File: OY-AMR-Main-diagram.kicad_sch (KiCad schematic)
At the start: 2 parts

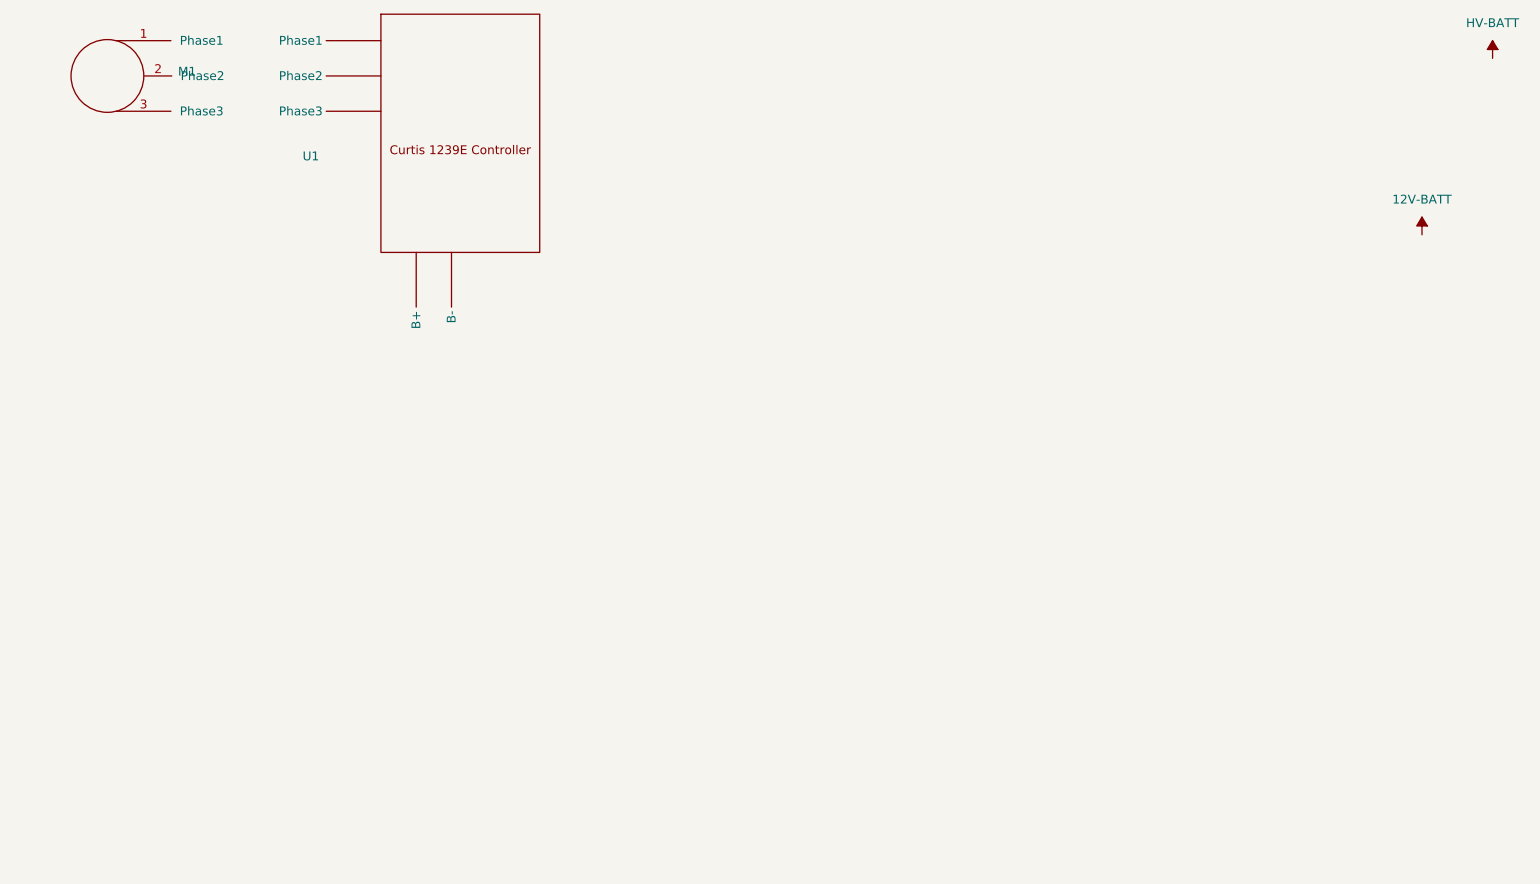
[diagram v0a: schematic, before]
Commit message: Added key switch component
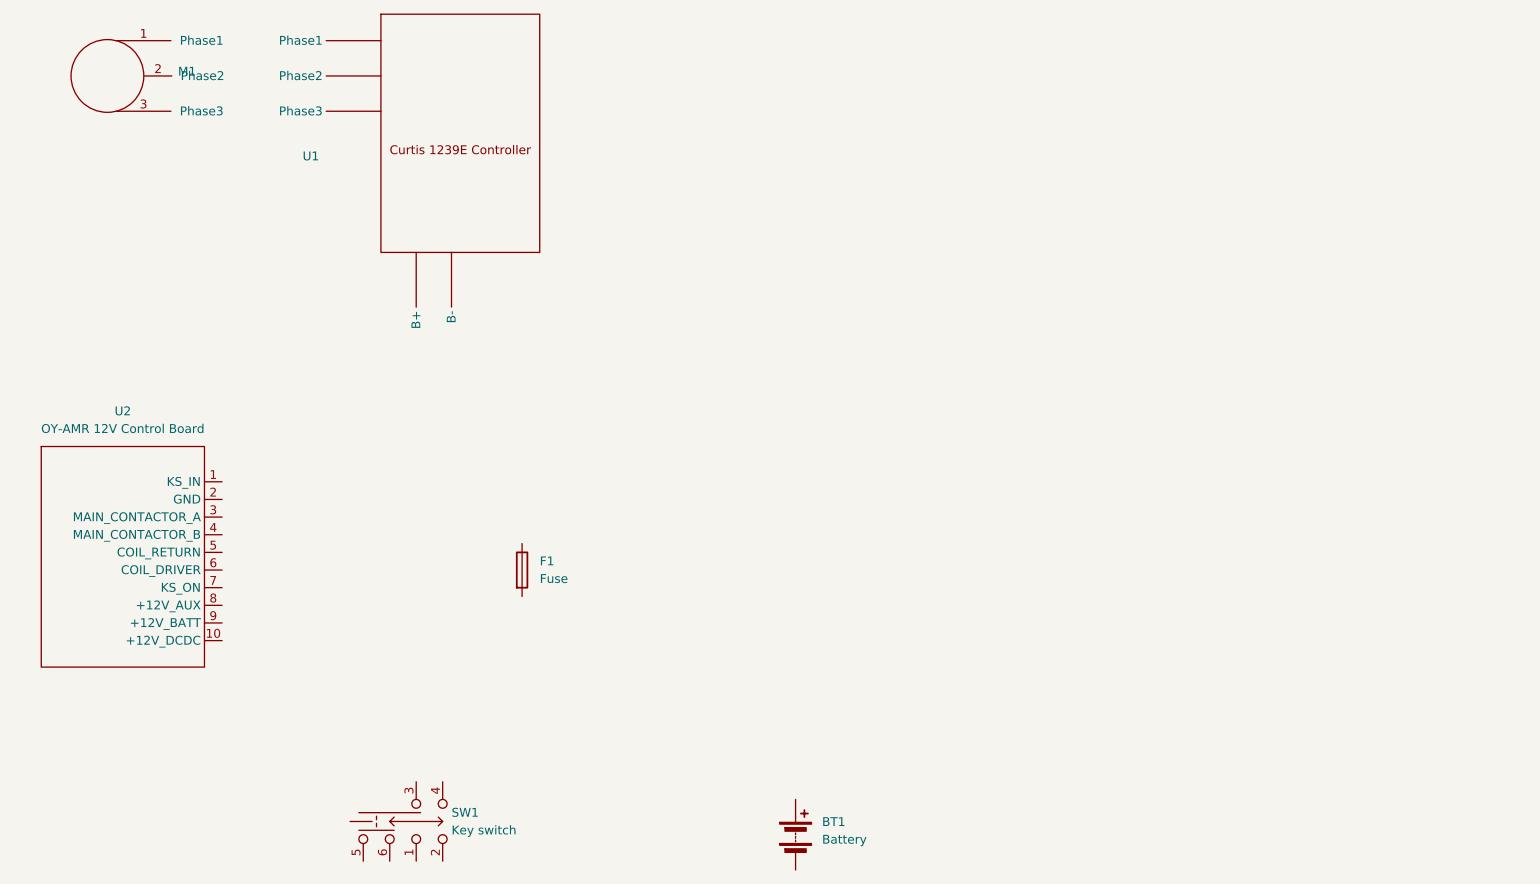
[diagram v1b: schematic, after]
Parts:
- added BT1: Battery, symbol Device:Battery
- added F1: Fuse, symbol Device:Fuse
- added SW1: Key switch, symbol OYAMR_Library:89165-01
- added U2: OY-AMR 12V Control Board, https://github.com/elfremdrift/OY-AMR-12V, symbol OYAMR_Library:Control_Board
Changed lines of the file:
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@@
 	(paper "A4")
+	(symbol
+		(lib_id "OYAMR_Library:Control_Board")
+		(at 52.07 92.71 0)
+		(unit 1)
+		(exclude_from_sim no)
+		(in_bom yes)
+		(on_board yes)
+		(dnp no)
+		(fields_autoplaced yes)
+		(property "Reference" "U2"
+			(at 46.6725 83.82 0)
+			(effects
+				(font
+					(size 1.27 1.27)
+				)
+			)
+		)
+		(property "Value" "OY-AMR 12V Control Board"
+			(at 46.6725 86.36 0)
+			(effects
+				(font
+					(size 1.27 1.27)
+				)
+			)
+		)
+		(property "Footprint" "https://github.com/elfremdrift/OY-AMR-12V"
+			(at 52.07 92.71 0)
+			(effects
+				(font
+					(size 1.27 1.27)
+				)
+				(hide yes)
+			)
+		)
+		(property "Datasheet" ""
+			(at 52.07 92.71 0)
+			(effects
+				(font
+					(size 1.27 1.27)
+				)
+				(hide yes)
+			)
+		)
+		(property "Description" ""
+			(at 52.07 92.71 0)
+			(effects
+				(font
+					(size 1.27 1.27)
+				)
+				(hide yes)
+			)
+		)
+		(pin "8"
+		)
+		(pin "3"
+		)
+		(pin "5"
+		)
+		(pin "7"
+		)
+		(pin "6"
+		)
+		(pin "4"
+		)
+		(pin "1"
+		)
+		(pin "2"
+		)
+		(pin "10"
+		)
+		(pin "9"
+		)
+		(instances
+			(project ""
+				(path "/ef01d6f9-a0de-44a4-9cac-f1674149af30"
+					(reference "U2")
+					(unit 1)
+				)
+			)
+		)
+	)
 	(symbol
 		(lib_id "OYAMR_Library:3_Phase_Motor")
@@
 	)
 	(symbol
-		(lib_id "power:-BATT")
-		(at 233.68 58.42 0)
-		(unit 1)
-		(exclude_from_sim no)
-		(in_bom yes)
-		(on_board yes)
-		(dnp no)
-		(fields_autoplaced yes)
-		(property "Reference" "#PWR02"
-			(at 233.68 62.23 0)
-			(effects
-				(font
-					(size 1.27 1.27)
-				)
-				(hide yes)
-			)
-		)
-		(property "Value" "12V-BATT"
-			(at 233.68 53.34 0)
-			(effects
-				(font
-					(size 1.27 1.27)
-				)
+		(lib_id "Device:Battery")
+		(at 143.51 144.78 0)
+		(unit 1)
+		(exclude_from_sim no)
+		(in_bom yes)
+		(on_board yes)
+		(dnp no)
+		(fields_autoplaced yes)
+		(property "Reference" "BT1"
+			(at 147.32 142.9384 0)
+			(effects
+				(font
+					(size 1.27 1.27)
+				)
+				(justify left)
+			)
+		)
+		(property "Value" "Battery"
+			(at 147.32 145.4784 0)
+			(effects
+				(font
+					(size 1.27 1.27)
+				)
+				(justify left)
 			)
 		)
 		(property "Footprint" ""
-			(at 233.68 58.42 0)
-			(effects
-				(font
-					(size 1.27 1.27)
-				)
-				(hide yes)
-			)
-		)
-		(property "Datasheet" ""
-			(at 233.68 58.42 0)
-			(effects
-				(font
-					(size 1.27 1.27)
-				)
-				(hide yes)
-			)
-		)
-		(property "Description" "Power symbol creates a global label with name \"-BATT\""
-			(at 233.68 58.42 0)
+			(at 143.51 143.256 90)
+			(effects
+				(font
+					(size 1.27 1.27)
+				)
+				(hide yes)
+			)
+		)
+		(property "Datasheet" "~"
+			(at 143.51 143.256 90)
+			(effects
+				(font
+					(size 1.27 1.27)
+				)
+				(hide yes)
+			)
+		)
+		(property "Description" "Multiple-cell battery"
+			(at 143.51 144.78 0)
 			(effects
 				(font
@@
 		(pin "1"
 		)
-		(instances
-			(project ""
-				(path "/ef01d6f9-a0de-44a4-9cac-f1674149af30"
-					(reference "#PWR02")
+		(pin "2"
+		)
+		(instances
+			(project ""
+				(path "/ef01d6f9-a0de-44a4-9cac-f1674149af30"
+					(reference "BT1")
+					(unit 1)
+				)
+			)
+		)
+	)
+	(symbol
+		(lib_id "Device:Fuse")
+		(at 104.14 106.68 0)
+		(unit 1)
+		(exclude_from_sim no)
+		(in_bom yes)
+		(on_board yes)
+		(dnp no)
+		(fields_autoplaced yes)
+		(property "Reference" "F1"
+			(at 106.68 105.4099 0)
+			(effects
+				(font
+					(size 1.27 1.27)
+				)
+				(justify left)
+			)
+		)
+		(property "Value" "Fuse"
+			(at 106.68 107.9499 0)
+			(effects
+				(font
+					(size 1.27 1.27)
+				)
+				(justify left)
+			)
+		)
+		(property "Footprint" ""
+			(at 102.362 106.68 90)
+			(effects
+				(font
+					(size 1.27 1.27)
+				)
+				(hide yes)
+			)
+		)
+		(property "Datasheet" "~"
+			(at 104.14 106.68 0)
+			(effects
+				(font
+					(size 1.27 1.27)
+				)
+				(hide yes)
+			)
+		)
+		(property "Description" "Fuse"
+			(at 104.14 106.68 0)
+			(effects
+				(font
+					(size 1.27 1.27)
+				)
+				(hide yes)
+			)
+		)
+		(pin "1"
+		)
+		(pin "2"
+		)
+		(instances
+			(project ""
+				(path "/ef01d6f9-a0de-44a4-9cac-f1674149af30"
+					(reference "F1")
+					(unit 1)
+				)
+			)
+		)
+	)
+	(symbol
+		(lib_id "OYAMR_Library:89165-01")
+		(at 87.63 143.51 0)
+		(unit 1)
+		(exclude_from_sim no)
+		(in_bom yes)
+		(on_board yes)
+		(dnp no)
+		(fields_autoplaced yes)
+		(property "Reference" "SW1"
+			(at 93.98 141.6049 0)
+			(effects
+				(font
+					(size 1.27 1.27)
+				)
+				(justify left)
+			)
+		)
+		(property "Value" "Key switch"
+			(at 93.98 144.1449 0)
+			(effects
+				(font
+					(size 1.27 1.27)
+				)
+				(justify left)
+			)
+		)
+		(property "Footprint" ""
+			(at 84.455 136.525 0)
+			(effects
+				(font
+					(size 1.27 1.27)
+				)
+				(hide yes)
+			)
+		)
+		(property "Datasheet" "~"
+			(at 84.455 136.525 0)
+			(effects
+				(font
+					(size 1.27 1.27)
+				)
+				(hide yes)
+			)
+		)
+		(property "Description" "Honywell key switch 6p off-on-start"
+			(at 87.63 143.51 0)
+			(effects
+				(font
+					(size 1.27 1.27)
+				)
+				(hide yes)
+			)
+		)
+		(pin "5"
+		)
+		(pin "2"
+		)
+		(pin "3"
+		)
+		(pin "4"
+		)
+		(pin "6"
+		)
+		(pin "1"
+		)
+		(instances
+			(project ""
+				(path "/ef01d6f9-a0de-44a4-9cac-f1674149af30"
+					(reference "SW1")
 					(unit 1)
 				)
@@
 					(unit 1)
 				)
-			)
-		)
-	)
-	(symbol
-		(lib_id "power:-BATT")
-		(at 243.84 33.02 0)
-		(unit 1)
-		(exclude_from_sim no)
-		(in_bom yes)
-		(on_board yes)
-		(dnp no)
-		(fields_autoplaced yes)
-		(property "Reference" "#PWR01"
-			(at 243.84 36.83 0)
-			(effects
-				(font
-					(size 1.27 1.27)
-				)
-				(hide yes)
-			)
-		)
-		(property "Value" "HV-BATT"
-			(at 243.84 27.94 0)
-			(effects
-				(font
-					(size 1.27 1.27)
-				)
-			)
-		)
-		(property "Footprint" ""
-			(at 243.84 33.02 0)
-			(effects
-				(font
-					(size 1.27 1.27)
-				)
-				(hide yes)
-			)
-		)
-		(property "Datasheet" ""
-			(at 243.84 33.02 0)
-			(effects
-				(font
-					(size 1.27 1.27)
-				)
-				(hide yes)
-			)
-		)
-		(property "Description" "Power symbol creates a global label with name \"-BATT\""
-			(at 243.84 33.02 0)
-			(effects
-				(font
-					(size 1.27 1.27)
-				)
-				(hide yes)
-			)
-		)
-		(pin "1"
-		)
-		(instances
-			(project ""
-				(path "/ef01d6f9-a0de-44a4-9cac-f1674149af30"
-					(reference "#PWR01")
-					(unit 1)
-				)

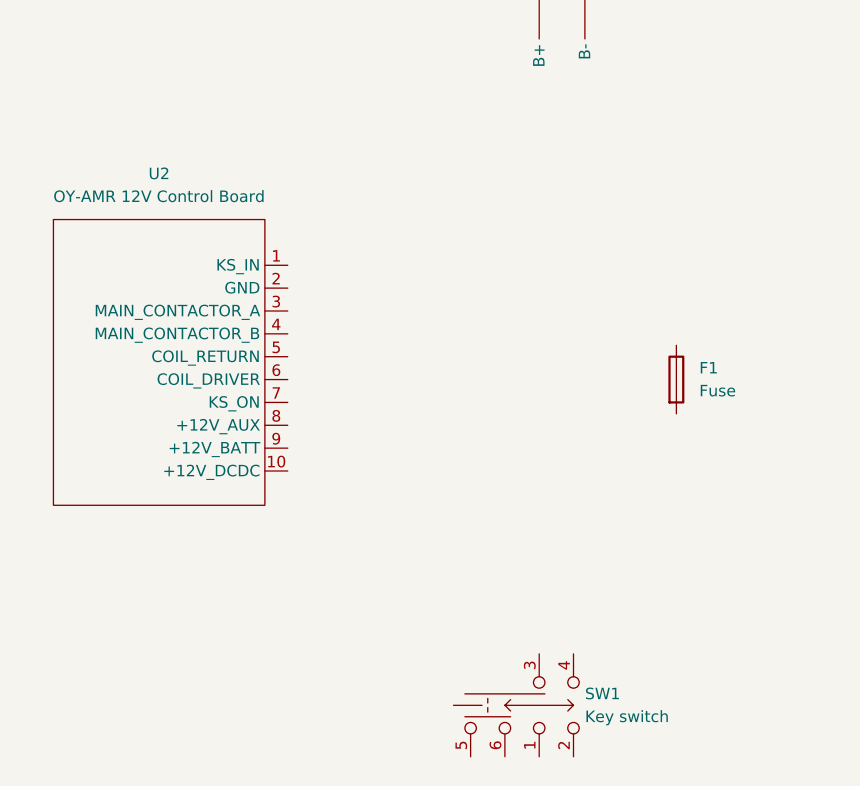
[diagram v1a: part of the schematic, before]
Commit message: removed unused comp.
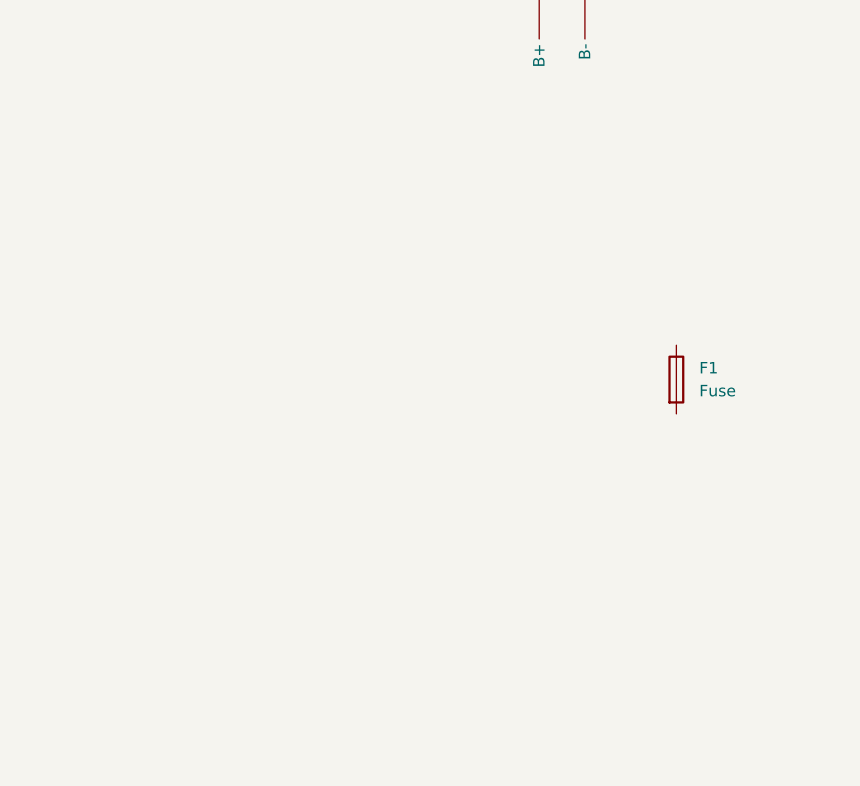
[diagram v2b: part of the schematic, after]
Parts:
- removed SW1: Key switch, symbol OYAMR_Library:89165-01
- removed U2: OY-AMR 12V Control Board, https://github.com/elfremdrift/OY-AMR-12V, symbol OYAMR_Library:Control_Board
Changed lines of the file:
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@@
 	(paper "A4")
-	(symbol
-		(lib_id "OYAMR_Library:Control_Board")
-		(at 52.07 92.71 0)
-		(unit 1)
-		(exclude_from_sim no)
-		(in_bom yes)
-		(on_board yes)
-		(dnp no)
-		(fields_autoplaced yes)
-		(property "Reference" "U2"
-			(at 46.6725 83.82 0)
-			(effects
-				(font
-					(size 1.27 1.27)
-				)
-			)
-		)
-		(property "Value" "OY-AMR 12V Control Board"
-			(at 46.6725 86.36 0)
-			(effects
-				(font
-					(size 1.27 1.27)
-				)
-			)
-		)
-		(property "Footprint" "https://github.com/elfremdrift/OY-AMR-12V"
-			(at 52.07 92.71 0)
-			(effects
-				(font
-					(size 1.27 1.27)
-				)
-				(hide yes)
-			)
-		)
-		(property "Datasheet" ""
-			(at 52.07 92.71 0)
-			(effects
-				(font
-					(size 1.27 1.27)
-				)
-				(hide yes)
-			)
-		)
-		(property "Description" ""
-			(at 52.07 92.71 0)
-			(effects
-				(font
-					(size 1.27 1.27)
-				)
-				(hide yes)
-			)
-		)
-		(pin "8"
-		)
-		(pin "3"
-		)
-		(pin "5"
-		)
-		(pin "7"
-		)
-		(pin "6"
-		)
-		(pin "4"
-		)
-		(pin "1"
-		)
-		(pin "2"
-		)
-		(pin "10"
-		)
-		(pin "9"
-		)
-		(instances
-			(project ""
-				(path "/ef01d6f9-a0de-44a4-9cac-f1674149af30"
-					(reference "U2")
-					(unit 1)
-				)
-			)
-		)
-	)
 	(symbol
 		(lib_id "OYAMR_Library:3_Phase_Motor")
@@
 					(unit 1)
 				)
-			)
-		)
-	)
-	(symbol
-		(lib_id "OYAMR_Library:89165-01")
-		(at 87.63 143.51 0)
-		(unit 1)
-		(exclude_from_sim no)
-		(in_bom yes)
-		(on_board yes)
-		(dnp no)
-		(fields_autoplaced yes)
-		(property "Reference" "SW1"
-			(at 93.98 141.6049 0)
-			(effects
-				(font
-					(size 1.27 1.27)
-				)
-				(justify left)
-			)
-		)
-		(property "Value" "Key switch"
-			(at 93.98 144.1449 0)
-			(effects
-				(font
-					(size 1.27 1.27)
-				)
-				(justify left)
-			)
-		)
-		(property "Footprint" ""
-			(at 84.455 136.525 0)
-			(effects
-				(font
-					(size 1.27 1.27)
-				)
-				(hide yes)
-			)
-		)
-		(property "Datasheet" "~"
-			(at 84.455 136.525 0)
-			(effects
-				(font
-					(size 1.27 1.27)
-				)
-				(hide yes)
-			)
-		)
-		(property "Description" "Honywell key switch 6p off-on-start"
-			(at 87.63 143.51 0)
-			(effects
-				(font
-					(size 1.27 1.27)
-				)
-				(hide yes)
-			)
-		)
-		(pin "5"
-		)
-		(pin "2"
-		)
-		(pin "3"
-		)
-		(pin "4"
-		)
-		(pin "6"
-		)
-		(pin "1"
-		)
-		(instances
-			(project ""
-				(path "/ef01d6f9-a0de-44a4-9cac-f1674149af30"
-					(reference "SW1")
-					(unit 1)
-				)
